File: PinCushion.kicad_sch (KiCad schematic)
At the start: 5 parts

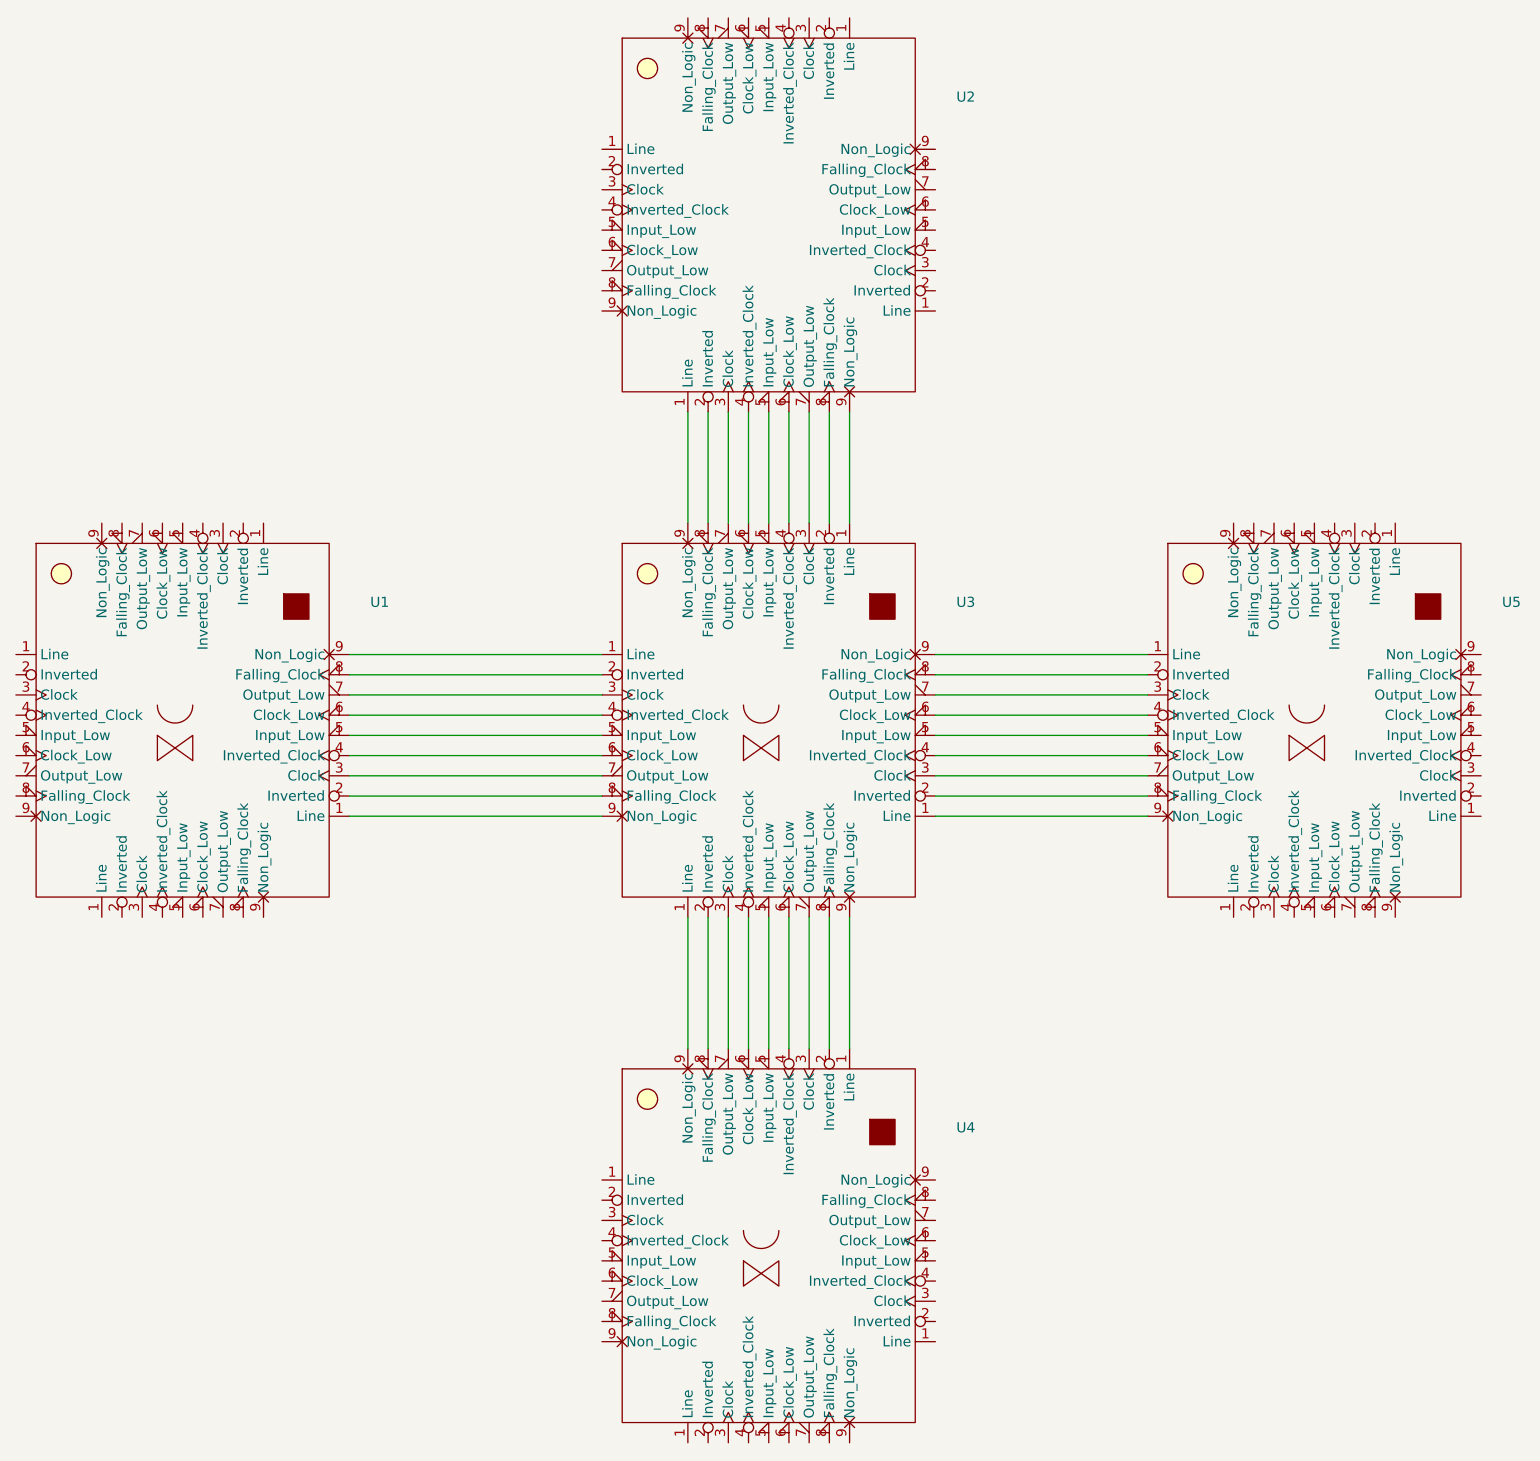
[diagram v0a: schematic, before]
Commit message: update pin numbers
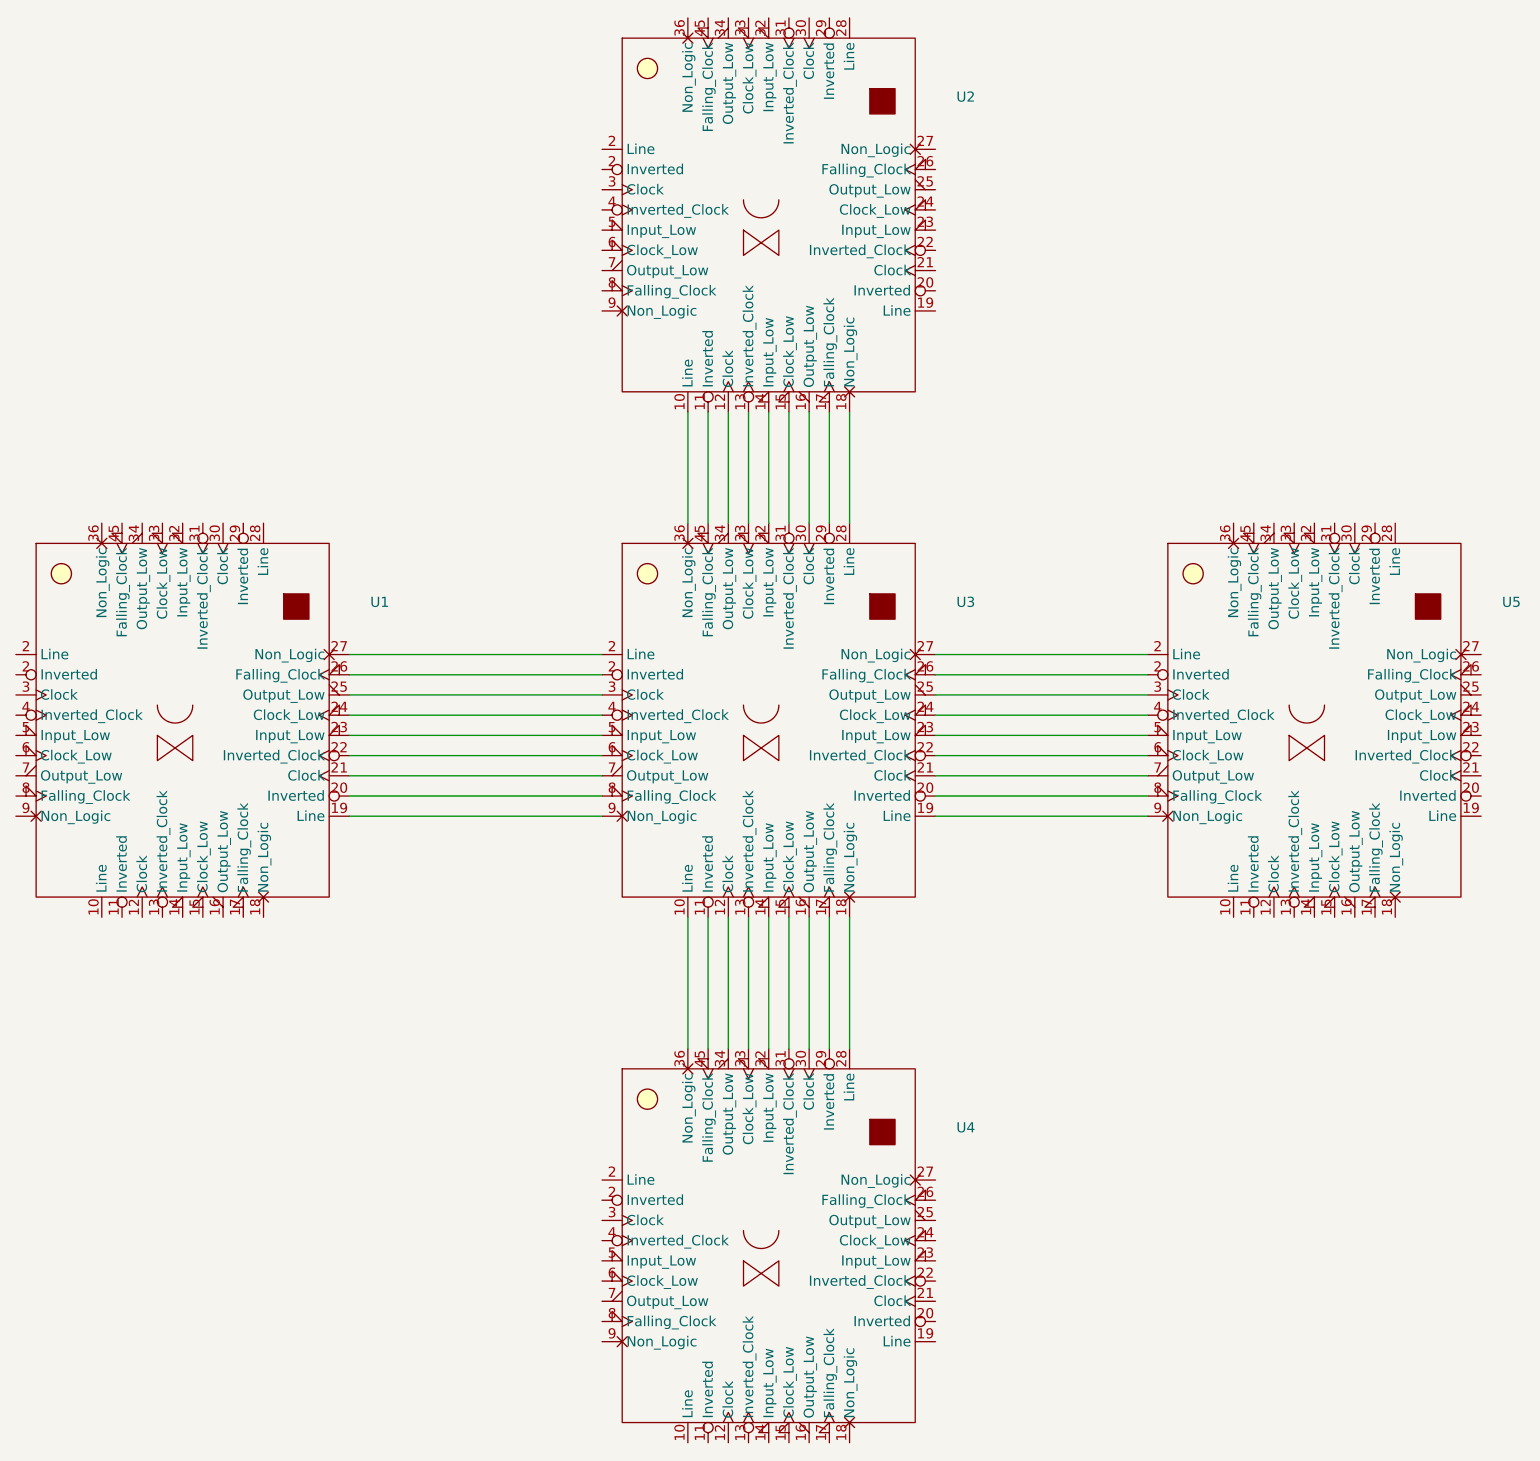
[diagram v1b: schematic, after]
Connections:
- net at U3.9 (Non_Logic): now also U1.19 (Line); no longer U2.1 (Line)
- net at U3.8 (Falling_Clock): now also U1.20 (Inverted); no longer U2.2 (Inverted)
- net at U3.7 (Output_Low): now also U1.21 (Clock); no longer U2.3 (Clock)
- net at U3.6 (Clock_Low): now also U1.22 (Inverted_Clock); no longer U2.4 (Inverted_Clock)
- net at U3.5 (Input_Low): now also U1.23 (Input_Low); no longer U2.5 (Input_Low)
- net at U3.4 (Inverted_Clock): now also U1.24 (Clock_Low); no longer U2.6 (Clock_Low)
- net at U3.3 (Clock): now also U1.25 (Output_Low); no longer U2.7 (Output_Low)
- net at U3.2 (Line): now also U1.27 (Non_Logic); no longer U2.8 (Falling_Clock)
- net at U5.9 (Non_Logic): now also U3.19 (Line); no longer U3.1 (Line)
- net at U4.9 (Non_Logic): no longer U3.1 (Line)
- net at U5.8 (Falling_Clock): now also U3.20 (Inverted); no longer U3.2 (Inverted)
- net at U4.8 (Falling_Clock): no longer U3.2 (Inverted)
- net at U5.7 (Output_Low): now also U3.21 (Clock); no longer U3.3 (Clock)
- net at U4.7 (Output_Low): no longer U3.3 (Clock)
- net at U5.6 (Clock_Low): now also U3.22 (Inverted_Clock); no longer U3.4 (Inverted_Clock)
- net at U4.6 (Clock_Low): no longer U3.4 (Inverted_Clock)
- net at U5.5 (Input_Low): now also U3.23 (Input_Low); no longer U3.5 (Input_Low)
- net at U4.5 (Input_Low): no longer U3.5 (Input_Low)
- net at U5.4 (Inverted_Clock): now also U3.24 (Clock_Low); no longer U3.6 (Clock_Low)
- net at U4.4 (Inverted_Clock): no longer U3.6 (Clock_Low)
- net at U5.3 (Clock): now also U3.25 (Output_Low); no longer U3.7 (Output_Low)
- net at U4.3 (Clock): no longer U3.7 (Output_Low)
- net at U5.2 (Line): now also U3.27 (Non_Logic); no longer U3.8 (Falling_Clock)
- net at U4.2 (Line): no longer U3.8 (Falling_Clock)
- new net: U2.10 (Line), U3.36 (Non_Logic)
- new net: U2.11 (Inverted), U3.45 (Falling_Clock)
- new net: U2.12 (Clock), U3.34 (Output_Low)
- new net: U2.13 (Inverted_Clock), U3.33 (Clock_Low)
- new net: U2.14 (Input_Low), U3.32 (Input_Low)
- new net: U2.15 (Clock_Low), U3.31 (Inverted_Clock)
- new net: U2.16 (Output_Low), U3.30 (Clock)
- new net: U2.17 (Falling_Clock), U3.29 (Inverted)
- new net: U2.18 (Non_Logic), U3.28 (Line)
- new net: U1.26 (Falling_Clock), U3.2 (Line)
- new net: U3.10 (Line), U4.36 (Non_Logic)
- new net: U3.11 (Inverted), U4.45 (Falling_Clock)
- new net: U3.12 (Clock), U4.34 (Output_Low)
- new net: U3.13 (Inverted_Clock), U4.33 (Clock_Low)
- new net: U3.14 (Input_Low), U4.32 (Input_Low)
- new net: U3.15 (Clock_Low), U4.31 (Inverted_Clock)
- new net: U3.16 (Output_Low), U4.30 (Clock)
- new net: U3.17 (Falling_Clock), U4.29 (Inverted)
- new net: U3.18 (Non_Logic), U4.28 (Line)
- new net: U3.26 (Falling_Clock), U5.2 (Line)
- now unconnected: U1.2 (Inverted), U1.3 (Clock), U1.4 (Inverted_Clock), U1.5 (Input_Low), U1.6 (Clock_Low), U1.7 (Output_Low), U1.8 (Falling_Clock), U1.9 (Non_Logic), U2.9 (Non_Logic)

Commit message: Update PinCushion.kicad_sch
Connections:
- net at U1.27 (Non_Logic): now also U3.1 (Line); no longer U3.2 (Line)
